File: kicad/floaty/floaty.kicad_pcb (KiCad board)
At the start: 2 copper layers, 30 x 115 mm, 29 parts, among them IC1 DW01A, J1 TYPE-C-31-M-12, Q1 FS8205A, Q2 AO3401A, U1 TP4056, U2 MPU-6050, U3 HT7333, U4 E73-2G4M08S1C

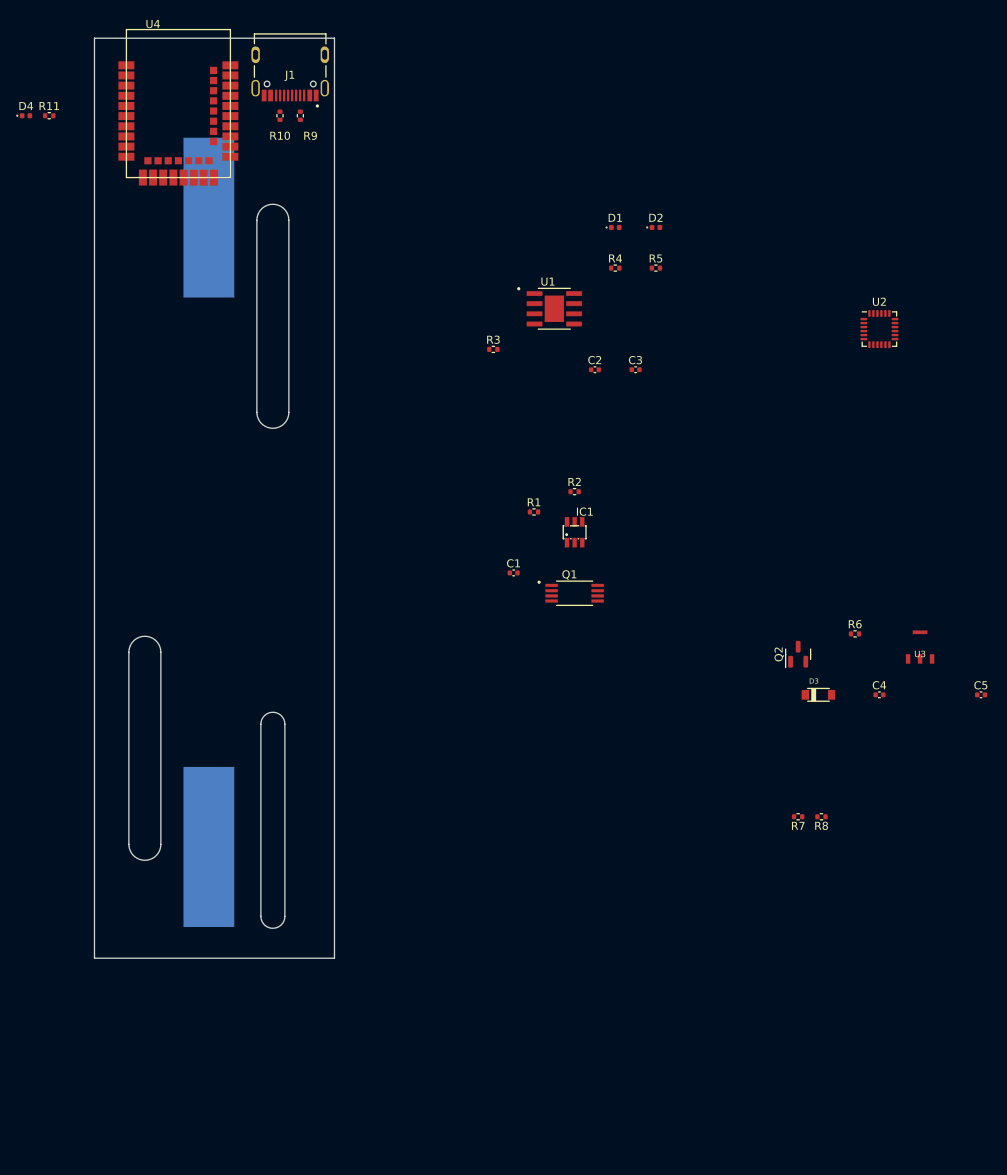
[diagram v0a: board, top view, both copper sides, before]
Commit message: First routing
Sort of works, but can be improved.
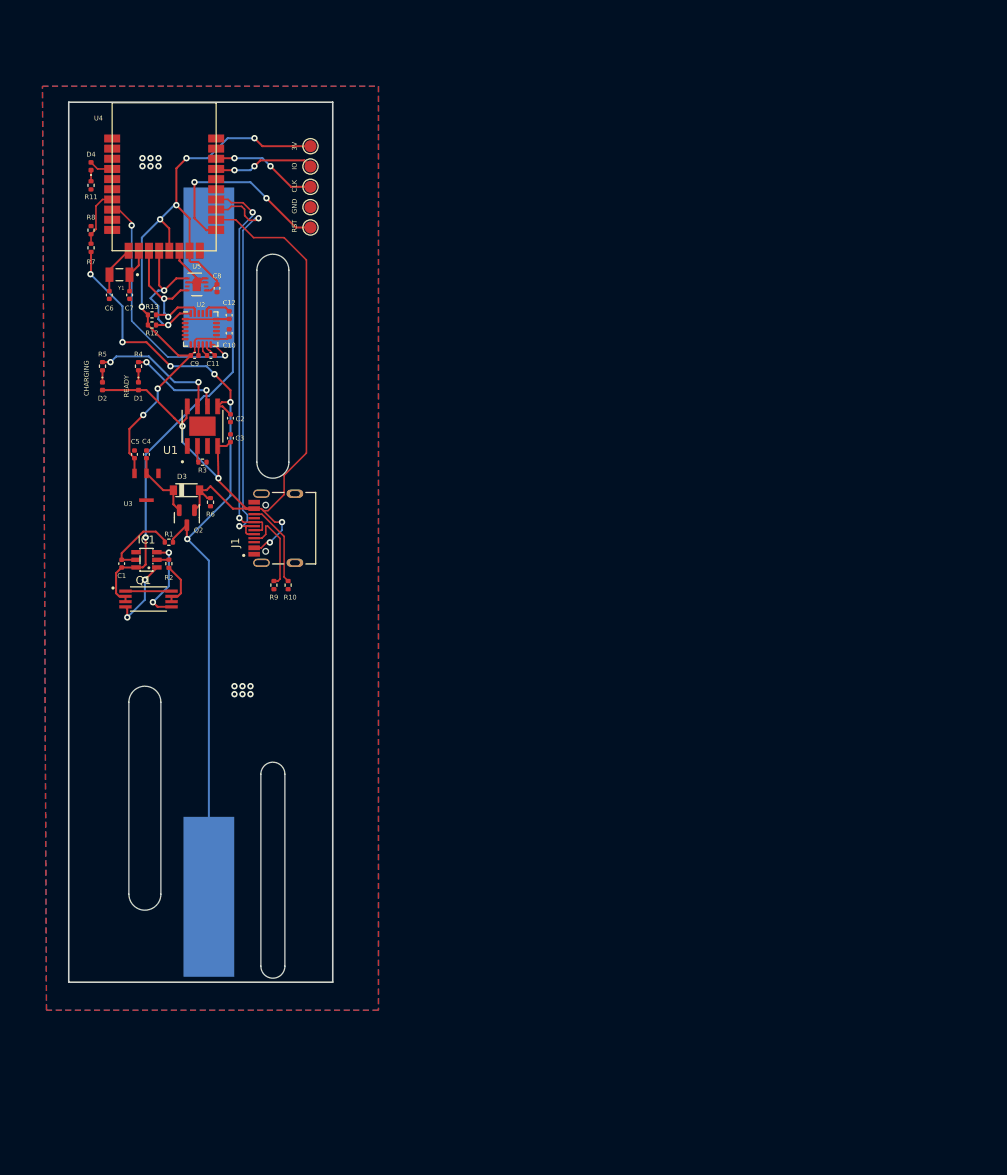
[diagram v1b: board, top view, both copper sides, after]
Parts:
- added C10: 0.1u, Capacitor_SMD:C_0402_1005Metric, F.Cu at (116.8, 86.9)
- added C11: 0.1u, Capacitor_SMD:C_0402_1005Metric, F.Cu at (114.6, 89.7)
- added C12: 2.2n, Capacitor_SMD:C_0402_1005Metric, F.Cu at (116.8, 84.6)
- added C6: 12p, Capacitor_SMD:C_0402_1005Metric, F.Cu at (101.9, 82.1)
- added C7: 12p, Capacitor_SMD:C_0402_1005Metric, F.Cu at (104.4, 82.1)
- added C8: 100n, Capacitor_SMD:C_0402_1005Metric, F.Cu at (115.3, 81.3)
- added C9: 10n, Capacitor_SMD:C_0402_1005Metric, F.Cu at (112.5, 89.7)
- added R12: 10k, Resistor_SMD:R_0402_1005Metric, F.Cu at (107.2, 85.9)
- added R13: 10k, Resistor_SMD:R_0402_1005Metric, F.Cu at (107.2, 84.6)
- added TP1: TestPoint, TestPoint:TestPoint_Pad_D1.5mm, F.Cu at (127.0, 73.7)
- added TP2: TestPoint, TestPoint:TestPoint_Pad_D1.5mm, F.Cu at (127.0, 71.1)
- added TP3: TestPoint, TestPoint:TestPoint_Pad_D1.5mm, F.Cu at (127.0, 68.6)
- added TP4: TestPoint, TestPoint:TestPoint_Pad_D1.5mm, F.Cu at (127.0, 66.0)
- added TP5: TestPoint, TestPoint:TestPoint_Pad_D1.5mm, F.Cu at (127.0, 63.5)
- added U5: SHT30-DIS, Sensor_Humidity:Sensirion_DFN-8-1EP_2.5x2.5mm_P0.5mm_EP1.1x1.7mm, F.Cu at (112.8, 80.8)
- added Y1: 32.768 kHz, lib:XTAL_NX3215SA-32.768K-STD-MUA-14, F.Cu at (103.1, 79.6)
- U4: footprint lib:E73-2G4M08S1C -> lib:E73-2G4M08S1C-modified
- moved R8 117.1 mm to (99.6, 74.0), turned to 90 degrees
- moved R7 113.5 mm to (99.6, 76.2), turned to 90 degrees
- moved C5 110.0 mm to (105.0, 102.0), turned to -90 degrees
- moved U3 99.2 mm to (106.5, 105.0), turned to 180 degrees
- moved C4 96.4 mm to (106.5, 102.0), turned to -90 degrees
- moved U2 84.8 mm to (113.3, 86.4)
- moved D3 83.0 mm to (111.5, 106.5)
- moved R6 82.2 mm to (114.5, 108.0), turned to -90 degrees
- moved Q2 78.3 mm to (111.5, 109.9), turned to -90 degrees
- moved D2 72.0 mm to (101.0, 93.5), turned to -90 degrees
- moved R5 70.3 mm to (101.0, 91.0), turned to 90 degrees
- moved D1 62.8 mm to (105.5, 93.5), turned to -90 degrees
- moved R4 60.8 mm to (105.5, 91.0), turned to 90 degrees
- moved J1 59.2 mm to (125.1, 111.3), turned to 90 degrees
- moved R9 58.8 mm to (122.4, 118.4)
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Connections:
- U1 pad 1: unconnected-(U1-Pad1) -> GND
- U2 pad 1: unconnected-(U2-Pad1) -> GND
- U2 pad 10: unconnected-(U2-Pad10) -> Net-(C11-Pad1)
- U2 pad 11: unconnected-(U2-Pad11) -> GND
- U2 pad 12: unconnected-(U2-Pad12) -> IMU_INT
- U2 pad 13: unconnected-(U2-Pad13) -> +3V0
- U2 pad 18: unconnected-(U2-Pad18) -> GND
- U2 pad 20: unconnected-(U2-Pad20) -> Net-(C12-Pad2)
- U2 pad 23: unconnected-(U2-Pad23) -> SCL
- U2 pad 24: unconnected-(U2-Pad24) -> SDA
- U2 pad 8: unconnected-(U2-Pad8) -> +3V0
- U2 pad 9: unconnected-(U2-Pad9) -> GND
- U4 pad 11: unconnected-(U4-Pad11) -> Net-(C6-Pad2)
- U4 pad 13: unconnected-(U4-Pad13) -> Net-(C7-Pad2)
- U4 pad 15: unconnected-(U4-Pad15) -> SCL
- U4 pad 17: unconnected-(U4-Pad17) -> SDA
- U4 pad 26: unconnected-(U4-Pad26) -> RESET
- U4 pad 37: unconnected-(U4-Pad37) -> SWDIO
- U4 pad 39: unconnected-(U4-Pad39) -> SWDCLK
- U4 pad 8: unconnected-(U4-Pad8) -> IMU_INT
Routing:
- net +5V: track 0.00 -> 105.0 mm, vias 0 -> 4
- net +BATT: track 0.00 -> 104.1 mm, vias 0 -> 6
- net +3V0: track 0.00 -> 90.9 mm, vias 0 -> 7
- net USB D-: track 0.00 -> 51.9 mm, vias 0 -> 2
- net Net-(BT1-Pad-): track 0.00 -> 51.9 mm, vias 0 -> 1
- net USB D+: track 0.00 -> 49.2 mm, vias 0 -> 2
- net IMU_INT: track 0.00 -> 31.4 mm, vias 0 -> 2
- net RESET: track 0.00 -> 24.7 mm, vias 0 -> 2
- net GND: track 0.00 -> 23.7 mm, vias 0 -> 12
- net SDA: track 0.00 -> 20.4 mm, vias 0 -> 2
- net SCL: track 0.00 -> 18.6 mm, vias 0 -> 2
- net Net-(R5-Pad2): track 0.00 -> 16.7 mm, vias 0 -> 2
- net SWDCLK: track 0.00 -> 13.3 mm, vias 0 -> 2
- net SWDIO: track 0.00 -> 12.7 mm, vias 0 -> 2
- net Net-(R4-Pad2): track 0.00 -> 11.8 mm, vias 0 -> 2
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- added copper zone on B.Cu, net GND
- added copper zone on F.Cu, net GND
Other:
- board size 30 x 115 mm -> 33 x 110 mm
- board text added: "3V"
- board text added: "CHARGING"
- board text added: "CLK"
- board text added: "GND"
- board text added: "IO"
- board text added: "READY"
- board text added: "RST"

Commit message: Better routing
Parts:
- added G***: LOGO, lib:battery-full, F.Cu at (106.6, 89.4)
- added G***: LOGO, lib:battery-half, F.Cu at (99.7, 89.4)
- added G***: LOGO, lib:sugarboat, F.Cu at (113.3, 121.0)
- added REF**: OSHW-Logo2_9.8x8mm_SilkScreen, Symbol:OSHW-Logo2_9.8x8mm_SilkScreen, F.Cu at (112.9, 163.3)
- added REF**: MountingHole_2.2mm_M2_DIN965_Pad, MountingHole:MountingHole_2.2mm_M2_DIN965_Pad, F.Cu at (119.0, 61.0)
- added REF**: MountingHole_2.2mm_M2_DIN965_Pad, MountingHole:MountingHole_2.2mm_M2_DIN965_Pad, F.Cu at (100.0, 165.0)
- added REF**: MountingHole_2.2mm_M2_DIN965_Pad, MountingHole:MountingHole_2.2mm_M2_DIN965_Pad, F.Cu at (126.0, 165.0)
- U3: value HT7333 -> HT7330
- moved R6 15.2 mm to (110.5, 93.3), turned to 90 degrees
- moved Q1 12.9 mm to (111.1, 108.0)
- moved Q2 11.7 mm to (107.3, 99.1)
- moved D3 11.7 mm to (107.3, 95.6)
- moved R10 11.4 mm to (117.3, 109.2), turned to 180 degrees
- moved C4 9.11 mm to (101.6, 94.3)
- moved C5 9.11 mm to (100.1, 94.3)
- moved U3 9.11 mm to (101.6, 97.3)
- moved C1 8.78 mm to (98.9, 108.1)
- moved IC1 8.78 mm to (102.0, 107.7)
- moved R2 8.48 mm to (105.4, 108.2)
- moved R1 7.97 mm to (105.4, 106.0), turned to -90 degrees
- moved R9 7.27 mm to (117.3, 113.2), turned to 180 degrees
- moved R4 4.70 mm to (104.8, 86.4), turned to 180 degrees
- moved R5 4.68 mm to (101.6, 86.4), turned to 180 degrees
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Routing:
- net +BATT: track 104.1 -> 120.9 mm, vias 6 -> 4
- net +3V0: track 90.9 -> 102.1 mm
- net Net-(BT1-Pad-): track 51.9 -> 61.6 mm, vias 1 -> 2
- net Net-(J1-PadB5): track 10.7 -> 1.53 mm
- net Net-(J1-PadA5): track 11.0 -> 2.37 mm
- net SCL: track 18.6 -> 13.0 mm
- net +5V: track 105.0 -> 100.7 mm
- net Net-(R4-Pad2): track 11.8 -> 16.0 mm
- net SDA: track 20.4 -> 16.4 mm
- net Net-(R5-Pad2): track 16.7 -> 19.6 mm
- net SWDCLK: track 13.3 -> 11.0 mm
- net Net-(IC1-Pad3): track 11.1 -> 13.3 mm
- net SWDIO: track 12.7 -> 10.6 mm
- net GND: track 23.7 -> 25.1 mm, vias 12 -> 18
- net Net-(D2-Pad1): track 1.50 -> 2.83 mm
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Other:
- board size 33 x 110 mm -> 34 x 110 mm
- board text added: "X"
- board text added: "Y"
- board text added: "Z"
- board text added: "v0.0.1a rbaron.net"
- board text removed: "CHARGING"
- board text removed: "READY"

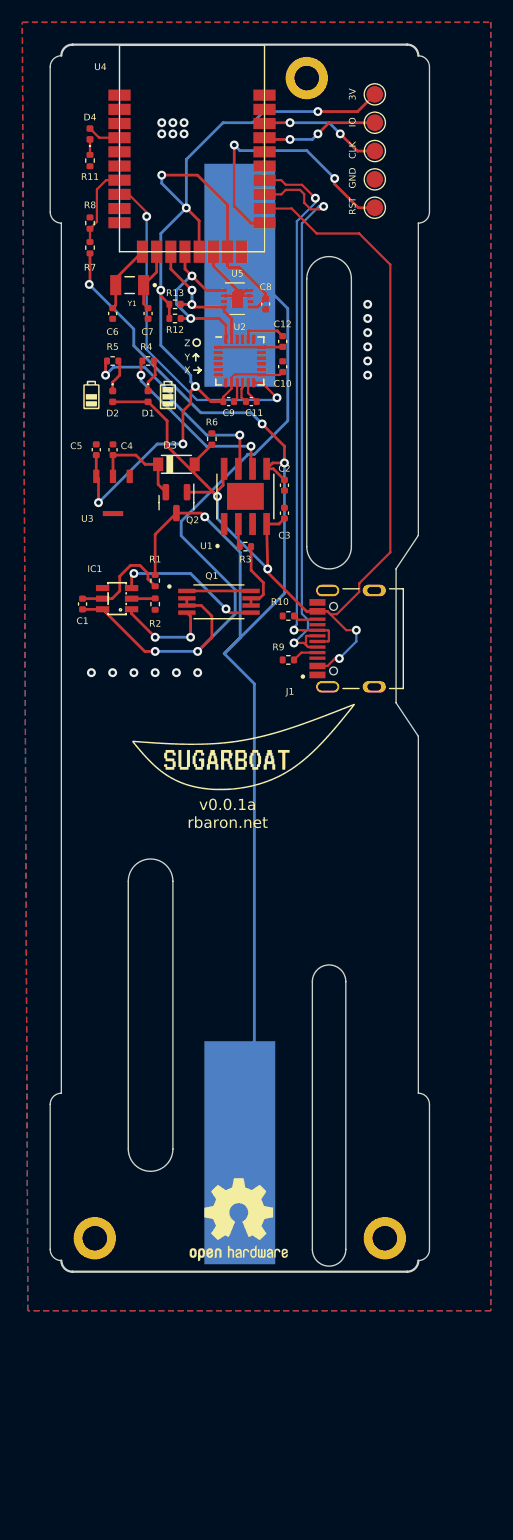
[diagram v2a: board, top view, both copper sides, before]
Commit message: Small fixes in the PCB layout & artwork
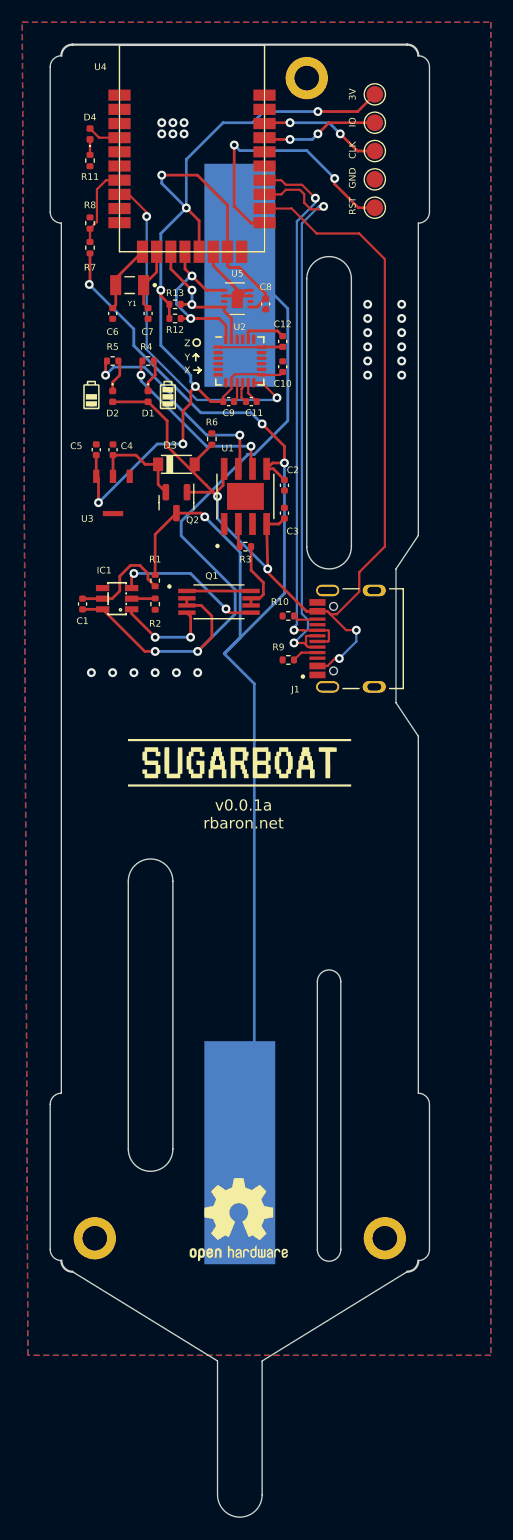
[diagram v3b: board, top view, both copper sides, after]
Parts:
- moved G*** 1.47 mm to (113.0, 122.4)
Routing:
- net GND: vias 18 -> 24
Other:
- board size 34 x 110 mm -> 34 x 132 mm

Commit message: Sent v0.0.0a PCB for fabrication
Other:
- board text added: "JLCJLCJLCJLC"
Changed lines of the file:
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@@
       (layerselection 0x00010fc_ffffffff)
       (disableapertmacros false)
-      (usegerberextensions false)
-      (usegerberattributes true)
-      (usegerberadvancedattributes true)
+      (usegerberextensions true)
+      (usegerberattributes false)
+      (usegerberadvancedattributes false)
       (creategerberjobfile true)
       (svguseinch false)
@@
       (psa4output false)
       (plotreference true)
-      (plotvalue true)
+      (plotvalue false)
       (plotinvisibletext false)
       (sketchpadsonfab false)
-      (subtractmaskfromsilk false)
+      (subtractmaskfromsilk true)
       (outputformat 1)
       (mirror false)
-      (drillshape 1)
+      (drillshape 0)
       (scaleselection 1)
-      (outputdirectory "")
+      (outputdirectory "gerber")
     )
   )
@@
     (effects (font (size 0.6 0.6) (thickness 0.15)))
   )
+  (gr_text "JLCJLCJLCJLC" (at 108.6104 62.611) (layer "F.SilkS")
+    (effects (font (size 1 1) (thickness 0.15)))
+  )
   (gr_text "GND" (at 123.1 69.96 90) (layer "F.SilkS")
